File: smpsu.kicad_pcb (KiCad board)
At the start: 2 copper layers, 23 x 47 mm, 12 parts, among them J1 Screw_Terminal_01x02, J2 Screw_Terminal_01x02, U1 LM2676SX-ADJ_NOPB

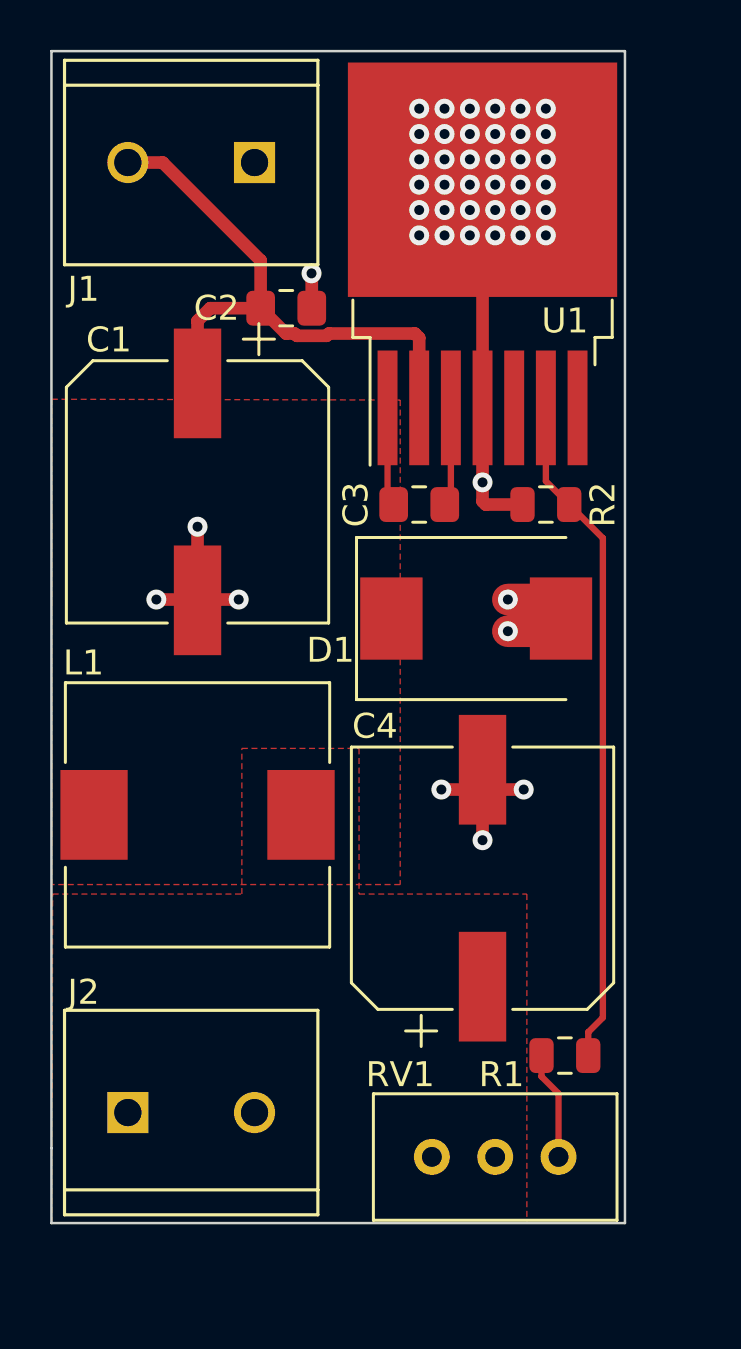
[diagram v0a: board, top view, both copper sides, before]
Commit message: WIP: redesign for better stability
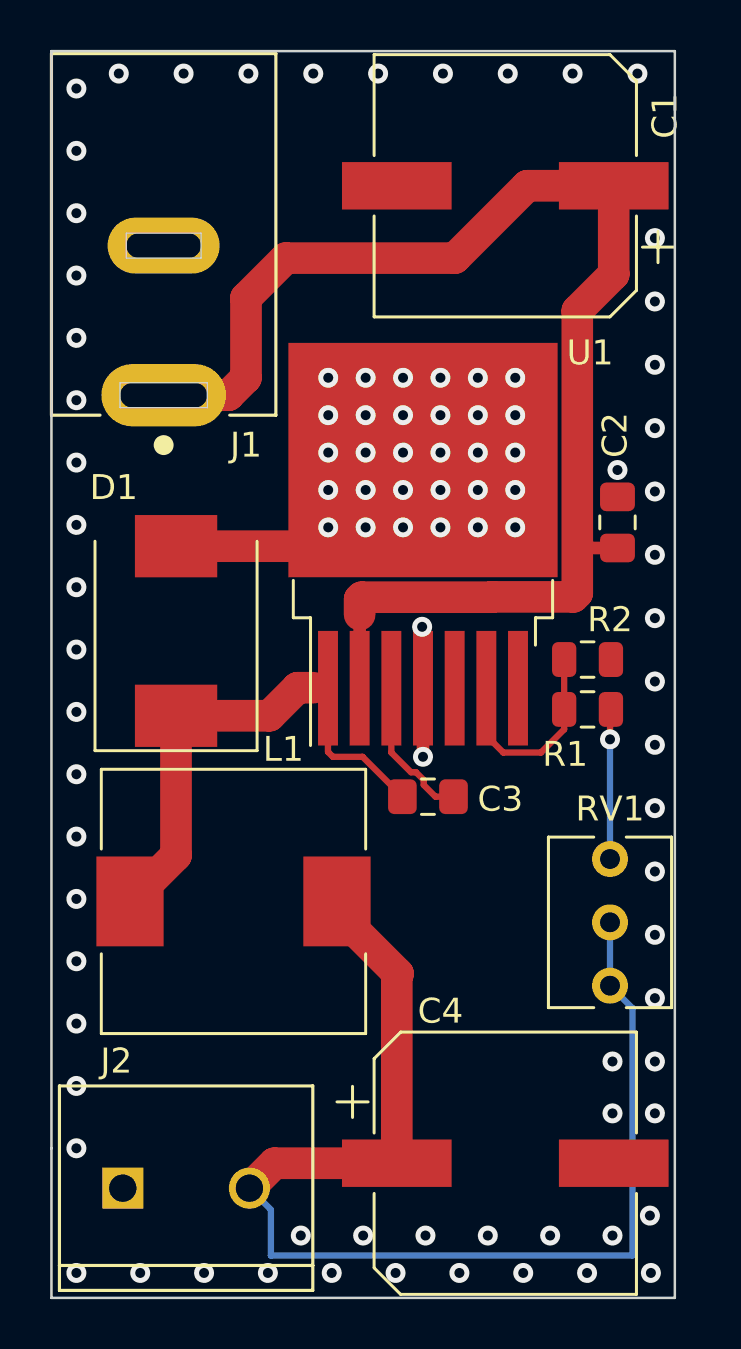
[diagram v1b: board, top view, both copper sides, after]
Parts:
- added ?: , , F.Cu at (150.5, 97.5)
- J1: value Screw_Terminal_01x02 -> PJ-037B; footprint 282837-2:TE_282837-2 -> Project:CUI_PJ-037B
- RV1: footprint Potentiometer_THT:Potentiometer_Bourns_3296W_Vertical -> Potentiometer_THT:Potentiometer_Vishay_T73XW_Horizontal
- moved C1 17.4 mm to (146.2, 62.4), turned to 180 degrees
- moved C2 15.8 mm to (150.7, 75.9), turned to 90 degrees
- moved R1 13.9 mm to (149.5, 83.4), turned to 180 degrees
- moved RV1 12.1 mm to (150.4, 89.4)
- moved D1 12.0 mm to (133.0, 80.3), turned to 90 degrees
- moved C3 11.7 mm to (143.1, 86.9)
- moved U1 11.5 mm to (142.9, 76.8)
- moved C4 11.5 mm to (146.2, 101.6), turned to 0 degrees
- moved J1 9.40 mm to (132.5, 70.8), turned to 90 degrees
- moved R2 6.44 mm to (149.5, 81.4), turned to 0 degrees
- moved L1 3.76 mm to (135.3, 91.1)
- moved J2 3.04 mm to (133.4, 102.6)
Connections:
- J1 pad 1: GND -> Net-(C1-Pad1)
- J1 pad 2: Net-(C1-Pad1) -> GND
- J2 pad 1: Net-(C4-Pad1) -> GND
- J2 pad 2: GND -> Net-(C4-Pad1)
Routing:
- net Net-(C4-Pad1): track 0.00 -> 49.1 mm
- net Net-(C1-Pad1): track 23.8 -> 54.4 mm
- net Net-(R1-Pad2): track 26.7 -> 8.49 mm
- net Net-(C3-Pad1): track 4.04 -> 20.5 mm
- net GND: track 32.4 -> 16.6 mm, vias 46 -> 94
- net Net-(C3-Pad2): track 4.04 -> 5.92 mm
- net Net-(R1-Pad1): track 4.35 -> 6.02 mm, vias 0 -> 1
- added copper zone on F.Cu, net GND
- removed copper zone on F.Cu, net Net-(C3-Pad1)
- removed copper zone on F.Cu, net Net-(C4-Pad1)
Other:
- board size 23 x 47 mm -> 25 x 50 mm
